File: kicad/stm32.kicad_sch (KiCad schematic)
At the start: 23 parts, among them P5 CONN_01X02, U2 TCAN334, U3 STM32G0B1CETxN, U6 24AA32, Y1 8MHz

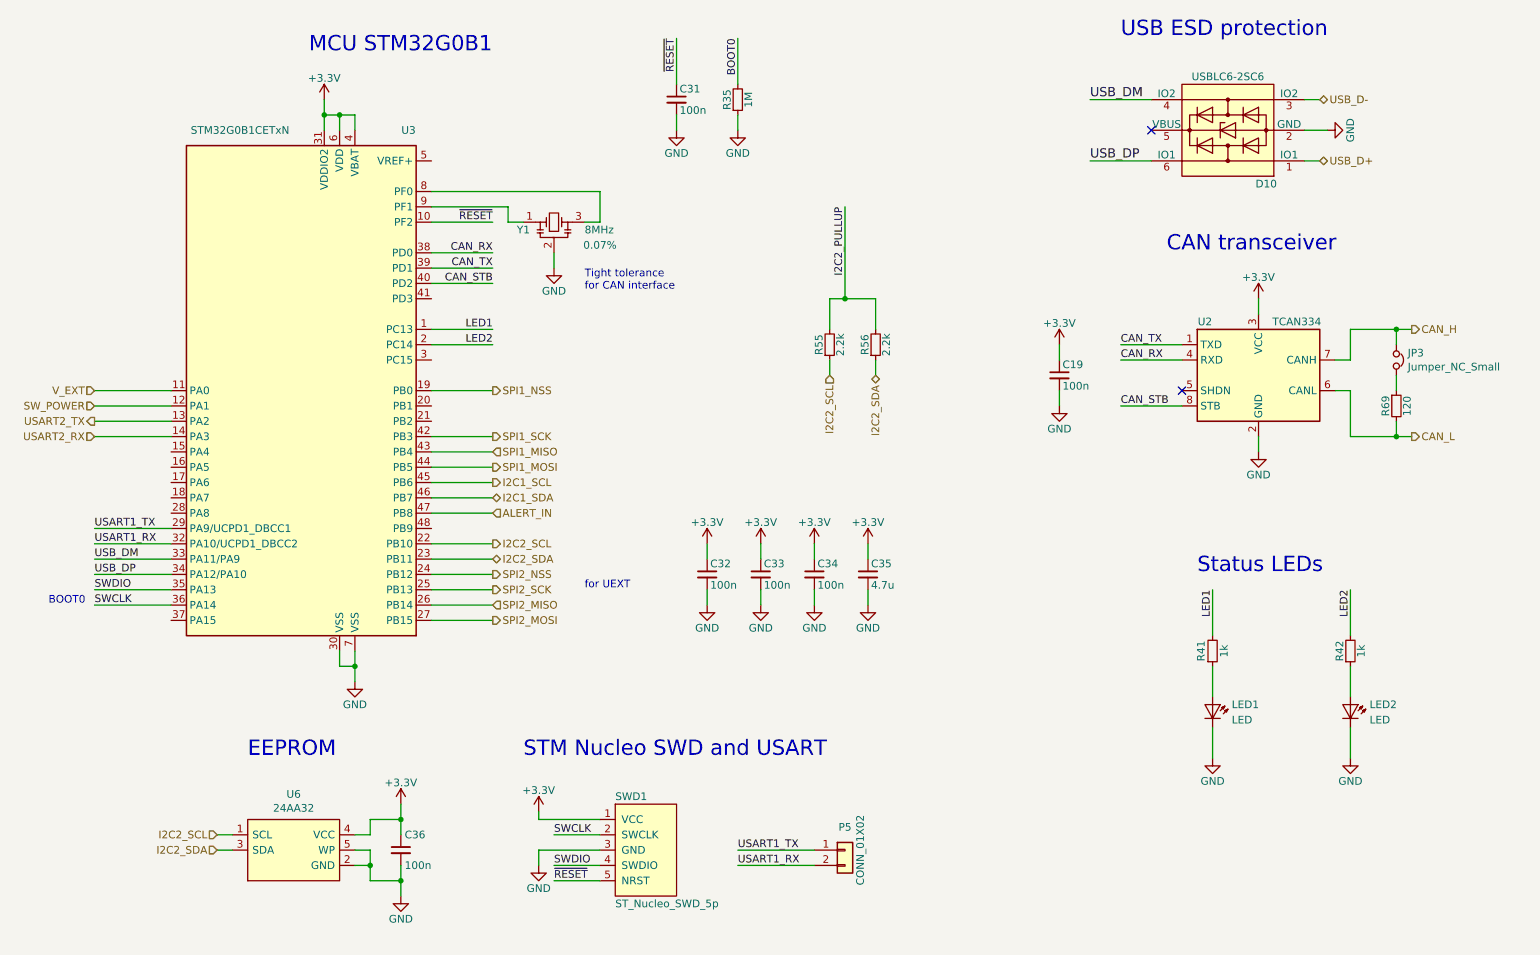
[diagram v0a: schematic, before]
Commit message: Update KiCad files based on spec updates
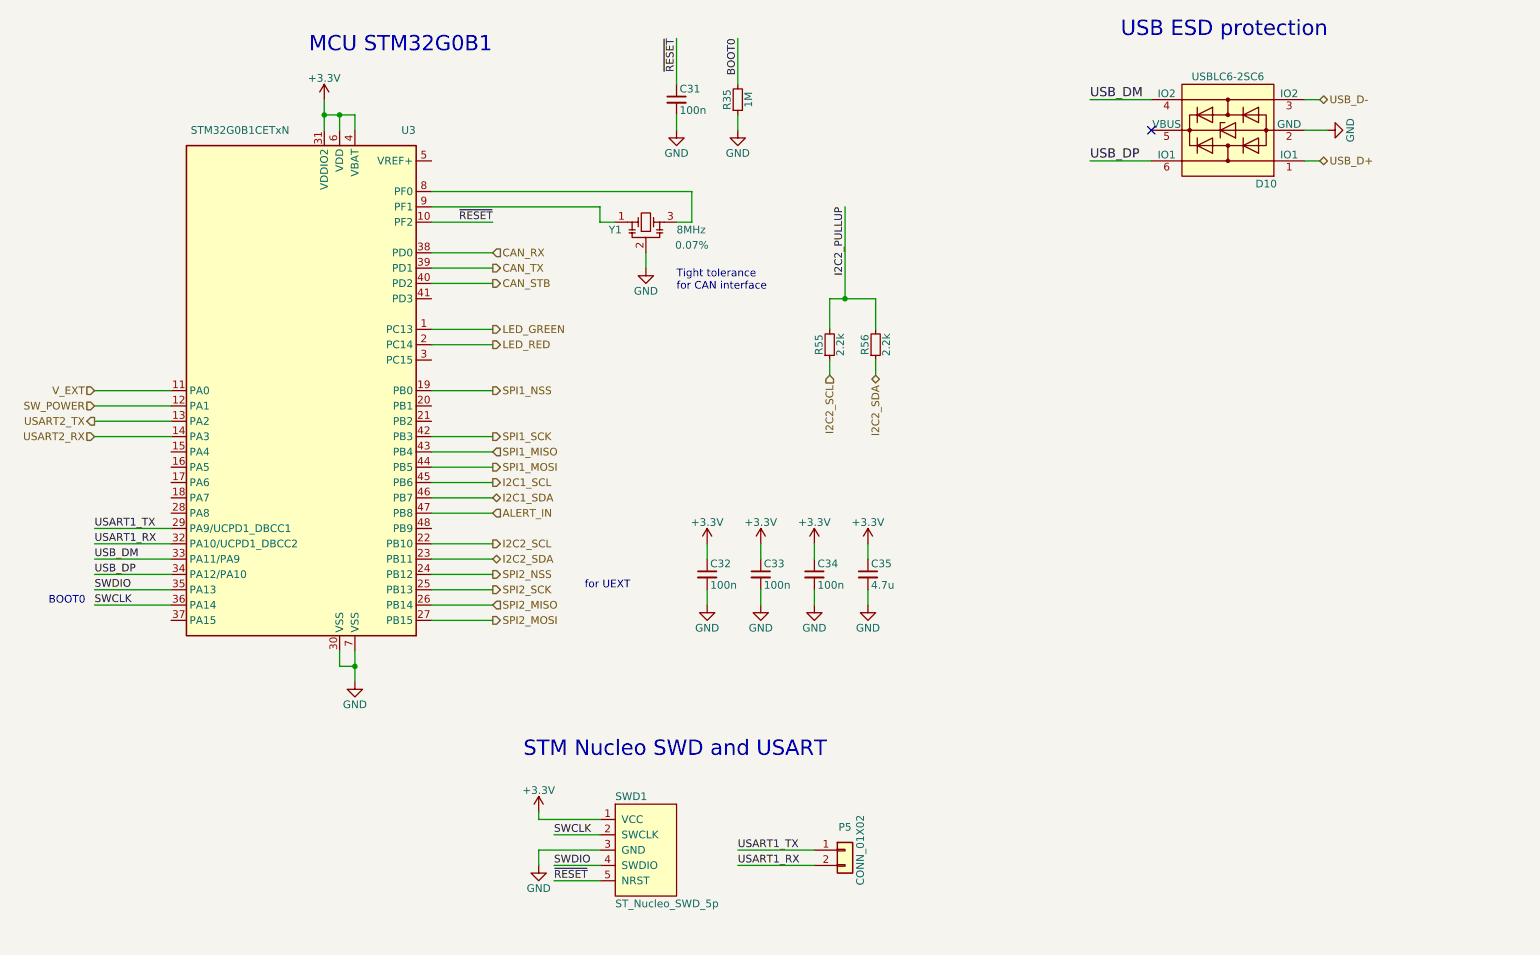
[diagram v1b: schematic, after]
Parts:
- removed C19, C36: 100n, LibreSolar:C_0603_1608, symbol LibreSolar:C
- removed JP3: Jumper_NC_Small, Connector_PinHeader_2.54mm:PinHeader_1x02_P2.54mm_Vertical, symbol LibreSolar:Jumper_NC_Small
- removed LED1, LED2: LED, LibreSolar:LED_0603_D3.0mm, symbol bms-control-16s-rescue:D_LED-LibreSolar
- removed R41, R42: 1k, LibreSolar:R_0603_1608, symbol LibreSolar:R
- removed R69: 120, LibreSolar:R_1206_3216, symbol LibreSolar:R
- removed U2: TCAN334, LibreSolar:SOIC-8_3.9x4.9mm_Pitch1.27mm, symbol Interface_CAN_LIN:TCAN334
- removed U6: 24AA32, LibreSolar:SOT-23-5, symbol bms-control-16s-rescue:24AA01-LibreSolar
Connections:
- net LED1 renamed LED_GREEN
- net LED2 renamed LED_RED
- no-connect marks 2 -> 1
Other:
- note removed: "CAN transceiver"
- note removed: "EEPROM"
- note removed: "Status LEDs"
- moved on the sheet: Y1

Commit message: WIP: Schematic almost finished
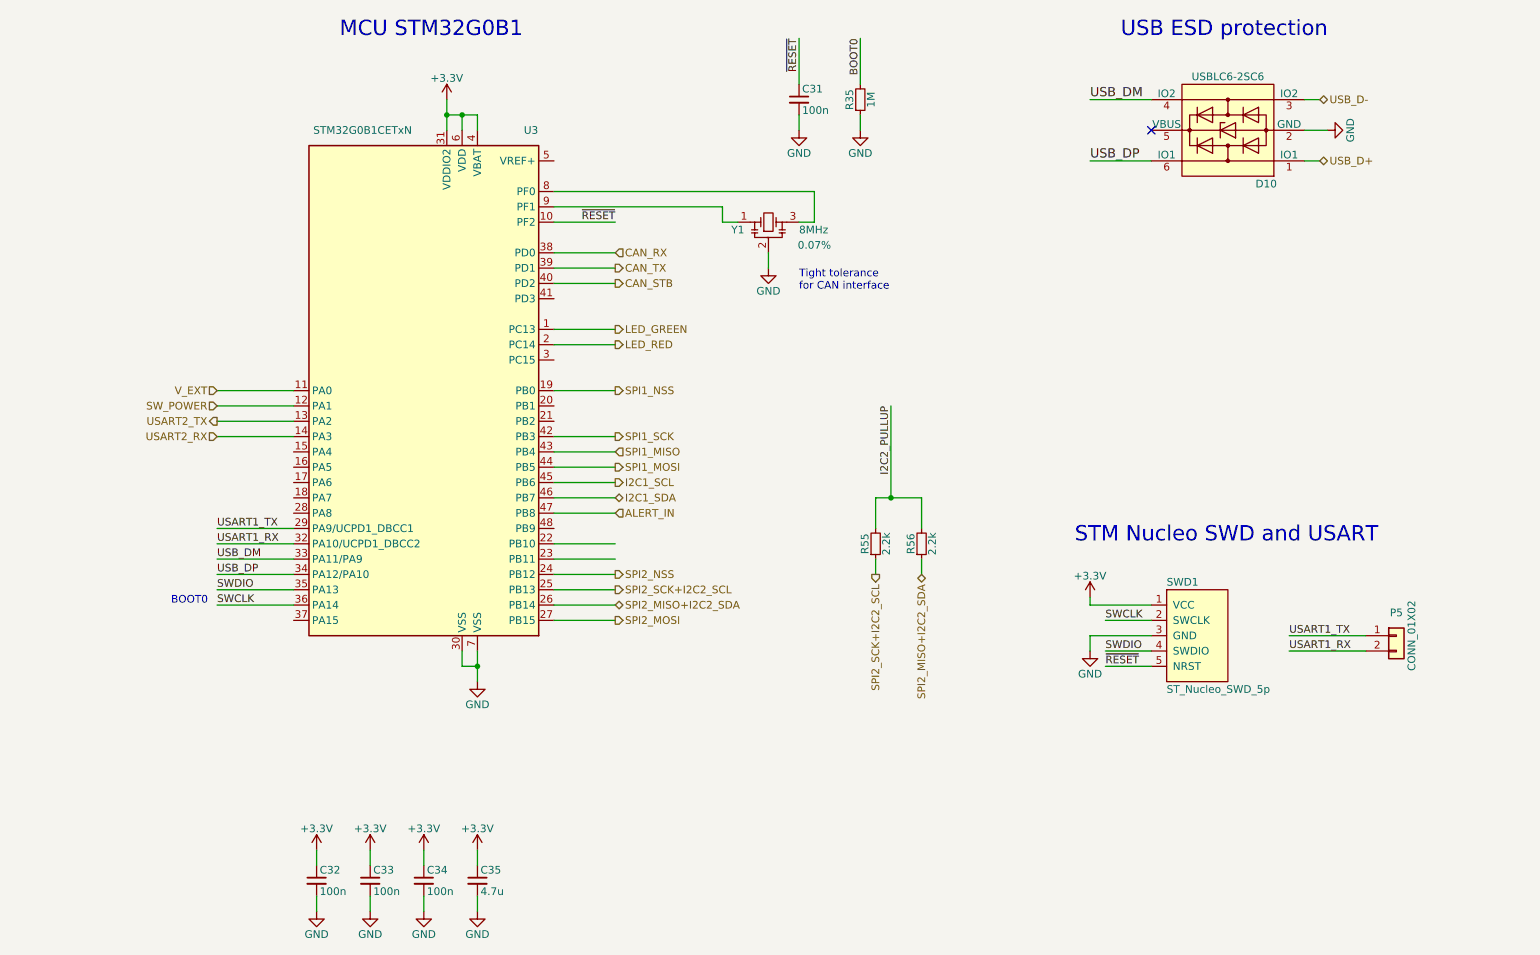
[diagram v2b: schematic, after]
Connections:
- net I2C2_SCL: no longer names the net of U3.22 (PB10)
- net I2C2_SCL: no longer R55.1
- net I2C2_SDA: no longer names the net of U3.23 (PB11)
- net I2C2_SDA: no longer R56.1
- net SPI2_MISO renamed SPI2_MISO+I2C2_SDA
- net SPI2_MISO+I2C2_SDA: now also R56.1
- net SPI2_SCK renamed SPI2_SCK+I2C2_SCL
- net SPI2_SCK+I2C2_SCL: now also R55.1
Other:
- note removed: "for UEXT"
- title: BMS 8S50 IC -> BMS 16S Control Board
- moved on the sheet: C31, C32, C33, C34, C35, P5, R35, R55, R56, SWD1, U3, Y1

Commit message: v0.1 design ready for review
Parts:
- removed C34: 100n, LibreSolar:C_0603_1608, symbol LibreSolar:C
- removed D10: USBLC6-2SC6, LibreSolar:SOT-23-6, symbol LibreSolar:USBLC6-2SC6
- removed P5: CONN_01X02, Connector_PinHeader_2.54mm:PinHeader_1x02_P2.54mm_Vertical, symbol Connector_Generic:Conn_01x02
- removed SWD1: ST_Nucleo_SWD_5p, Connector_PinHeader_2.54mm:PinHeader_1x05_P2.54mm_Vertical, symbol LibreSolar:ST_Nucleo_SWD_5p
- C31, C32, C33: value 100n -> 100nF; Manufacturer Yageo -> any; PartNumber CC0603KRX7R9BB104 -> (none)
- C35: value 4.7u -> 4.7µF
- R35: Manufacturer Yageo -> any; PartNumber RC0603FR-071ML -> (none)
- R55, R56: Manufacturer Yageo -> any; PartNumber RC0603FR-072K2L -> (none)
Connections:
- net I2C2_PULLUP is gone; now on net +3V3: R55.2, R56.2
- net SWCLK is gone; now on net SWDCLK: U3.36 (PA14)
- net USB_DM is gone; now on net USB_D-: U3.33 (PA11/PA9)
- net USB_DP is gone; now on net USB_D+: U3.34 (PA12/PA10)
- net BQ_SHUT: now reaches U3.20 (PB1)
- net BOOT0 renamed SWDCLK
- no-connect marks 1 -> 13
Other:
- note removed: "STM Nucleo SWD and USART"
- note removed: "USB ESD protection"
- moved on the sheet: C31, C32, C33, C35, R35, R55, R56, U3, Y1

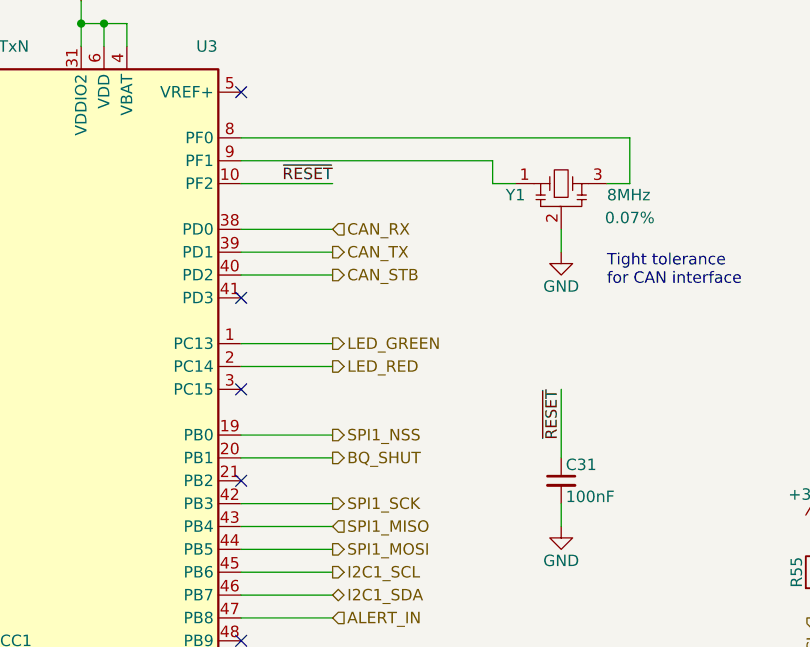
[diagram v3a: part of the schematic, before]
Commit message: Updates based on review comments (v0.2)
This is the design revision that was ordered for the first prototype build.

The pinout of the cell connector and the board-to-board connector changed
compared to v0.1, hence it got a minor revision update.

The control board is now a 4-layer board to improve the grounding of the
PCB. Various other suggested improvements from the design review are also
included in this update.

Fixes #11, #12, #13, #17, #18, #19
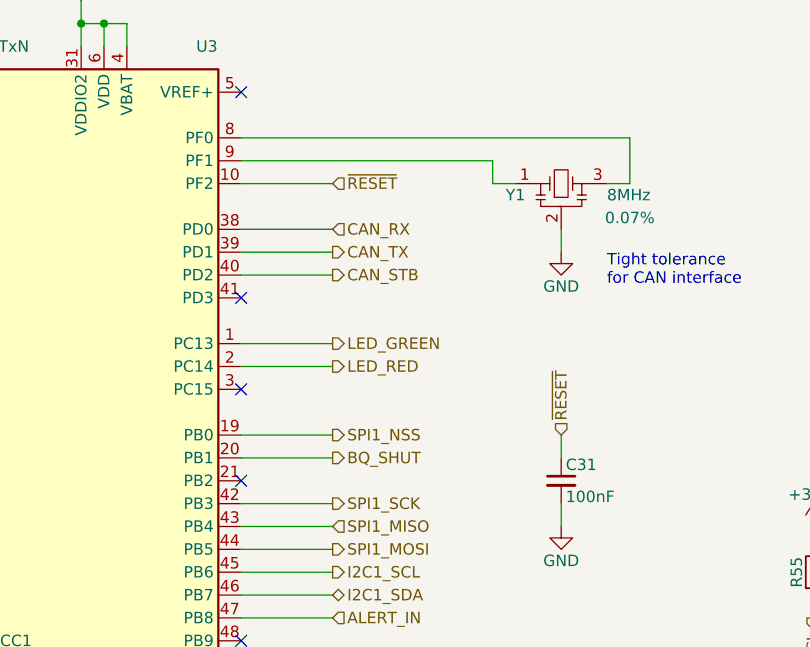
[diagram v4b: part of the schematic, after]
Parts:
- U3: Manufacturer (none) -> ST Microelectronics; PartNumber (none) -> STM32G0B1CET6N
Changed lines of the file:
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@@
   (title_block
     (title "BMS 16S Control Board")
-    (date "2022-02-24")
-    (rev "0.1")
+    (date "2022-03-15")
+    (rev "0.2")
     (company "Libre Solar Technologies GmbH")
     (comment 1 "Website: https://libre.solar")
@@
     (stroke (width 0) (type solid) (color 0 0 0 0))
   )
-  (wire (pts (xy 162.56 86.36) (xy 162.56 93.98))
+  (wire (pts (xy 162.56 91.44) (xy 162.56 93.98))
     (stroke (width 0) (type solid) (color 0 0 0 0))
   )
@@
     (effects (font (size 1.27 1.27)) (justify left bottom))
   )
-  (label "~{RESET}" (at 137.16 63.5 180)
-    (effects (font (size 1.27 1.27)) (justify right bottom))
-  )
-  (label "~{RESET}" (at 162.56 86.36 270)
-    (effects (font (size 1.27 1.27)) (justify right bottom))
-  )
   (hierarchical_label "USART2_RX" (shape input) (at 71.12 99.06 180)
     (effects (font (size 1.27 1.27)) (justify right))
@@
     (effects (font (size 1.27 1.27)) (justify left))
   )
+  (hierarchical_label "~{RESET}" (shape input) (at 137.16 63.5 0)
+    (effects (font (size 1.27 1.27)) (justify left))
+  )
   (hierarchical_label "USART1_TX" (shape output) (at 71.12 114.3 180)
     (effects (font (size 1.27 1.27)) (justify right))
@@
   )
   (hierarchical_label "BQ_SHUT" (shape output) (at 137.16 93.98 0)
+    (effects (font (size 1.27 1.27)) (justify left))
+  )
+  (hierarchical_label "~{RESET}" (shape input) (at 162.56 91.44 90)
     (effects (font (size 1.27 1.27)) (justify left))
   )
@@
       (effects (font (size 1.27 1.27)) hide)
     )
+    (property "Manufacturer" "ST Microelectronics" (id 4) (at 104.14 91.44 0)
+      (effects (font (size 1.27 1.27)) hide)
+    )
+    (property "PartNumber" "STM32G0B1CET6N" (id 5) (at 104.14 91.44 0)
+      (effects (font (size 1.27 1.27)) hide)
+    )
